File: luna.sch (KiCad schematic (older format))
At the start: 21 parts

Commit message: Almost finished.
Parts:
- C1, C2: renamed from C?; footprint (none) -> Capacitor_SMD:C_1206_3216Metric_Pad1.42x1.75mm_HandSolder
- J1: renamed from J?; footprint (none) -> Connector_PinHeader_2.54mm:PinHeader_1x06_P2.54mm_Horizontal
- J2: renamed from J?; footprint (none) -> Connector_Molex:Molex_Mini-Fit_Jr_5569-20A2_2x10_P4.20mm_Horizontal
- J3: renamed from J?; footprint (none) -> Connector_PinHeader_2.54mm:PinHeader_1x02_P2.54mm_Horizontal
- J4, J5, J6: renamed from Q?; footprint (none) -> Connector_PinHeader_2.54mm:PinHeader_1x02_P2.54mm_Horizontal
- R1, R2, R3, R4, R5, R6: renamed from R?; footprint (none) -> Resistor_SMD:R_0805_2012Metric_Pad1.15x1.40mm_HandSolder
- U1: renamed from U?; footprint (none) -> Package_TO_SOT_SMD:SOT-223-3_TabPin2
- gave numbers to parts that had none: 6
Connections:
- wire segments 79 -> 80
- no-connect marks 25 -> 40

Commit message: Second revision with on-board led swithes and dummy load output.
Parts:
- removed J2: Conn_02x10_Top_Bottom, Connector_Molex:Molex_Mini-Fit_Jr_5569-20A2_2x10_P4.20mm_Horizontal, symbol Connector_Generic:Conn_02x10_Top_Bottom
- removed J3, J4: Conn_01x02_Male, Connector_PinHeader_2.54mm:PinHeader_1x02_P2.54mm_Horizontal, symbol Connector:Conn_01x02_Male
- removed Q2, Q3: 2N7002, Package_TO_SOT_SMD:SOT-23, symbol Transistor_FET:2N7002
- removed R1: 10k, Resistor_SMD:R_0805_2012Metric_Pad1.15x1.40mm_HandSolder, symbol Device:R
- removed R3, R4: 1k, Resistor_SMD:R_0805_2012Metric_Pad1.15x1.40mm_HandSolder, symbol Device:R
- added C1, C4, C5, C6: 10u, Capacitor_SMD:C_1206_3216Metric_Pad1.42x1.75mm_HandSolder, symbol Device:C
- added D1, D2, D3: D_Schottky, Diode_SMD:D_SOD-323_HandSoldering, symbol Device:D_Schottky
- added J2: Conn_02x12_Top_Bottom, Connector_Molex:Molex_Mini-Fit_Jr_5569-24A2_2x12_P4.20mm_Horizontal, symbol Connector_Generic:Conn_02x12_Top_Bottom
- added J5: Screw_Terminal_01x06, TerminalBlock_RND:TerminalBlock_RND_205-00291_1x06_P5.08mm_Horizontal, symbol Connector:Screw_Terminal_01x06
- added Q4, Q5, Q6: DMN3404L, Package_TO_SOT_SMD:SOT-23, symbol Transistor_FET:DMN3404L
- added R10, R2, R8, R9: 10k, Resistor_SMD:R_0805_2012Metric_Pad1.15x1.40mm_HandSolder, symbol Device:R
- added R5, R6, R7: 100, Resistor_SMD:R_0805_2012Metric_Pad1.15x1.40mm_HandSolder, symbol Device:R
- R1: renamed from R5; value 10k -> 1k
- R3: renamed from R6; value 10k -> 1k
- renumbered C1 to C2, C2 to C3, J5 to J3, J6 to J4, Q4 to Q1, Q1 to Q2, Q5 to Q3, R2 to R4
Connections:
- net labels added: DUMMY_LOAD, DUMMY_LOAD_OUT, GNDPWR, LED_W1_OUT, LED_W2_OUT
- wire segments 80 -> 135
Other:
- moved on the sheet: J3, J4, Q1, Q2, Q3, R1, R3

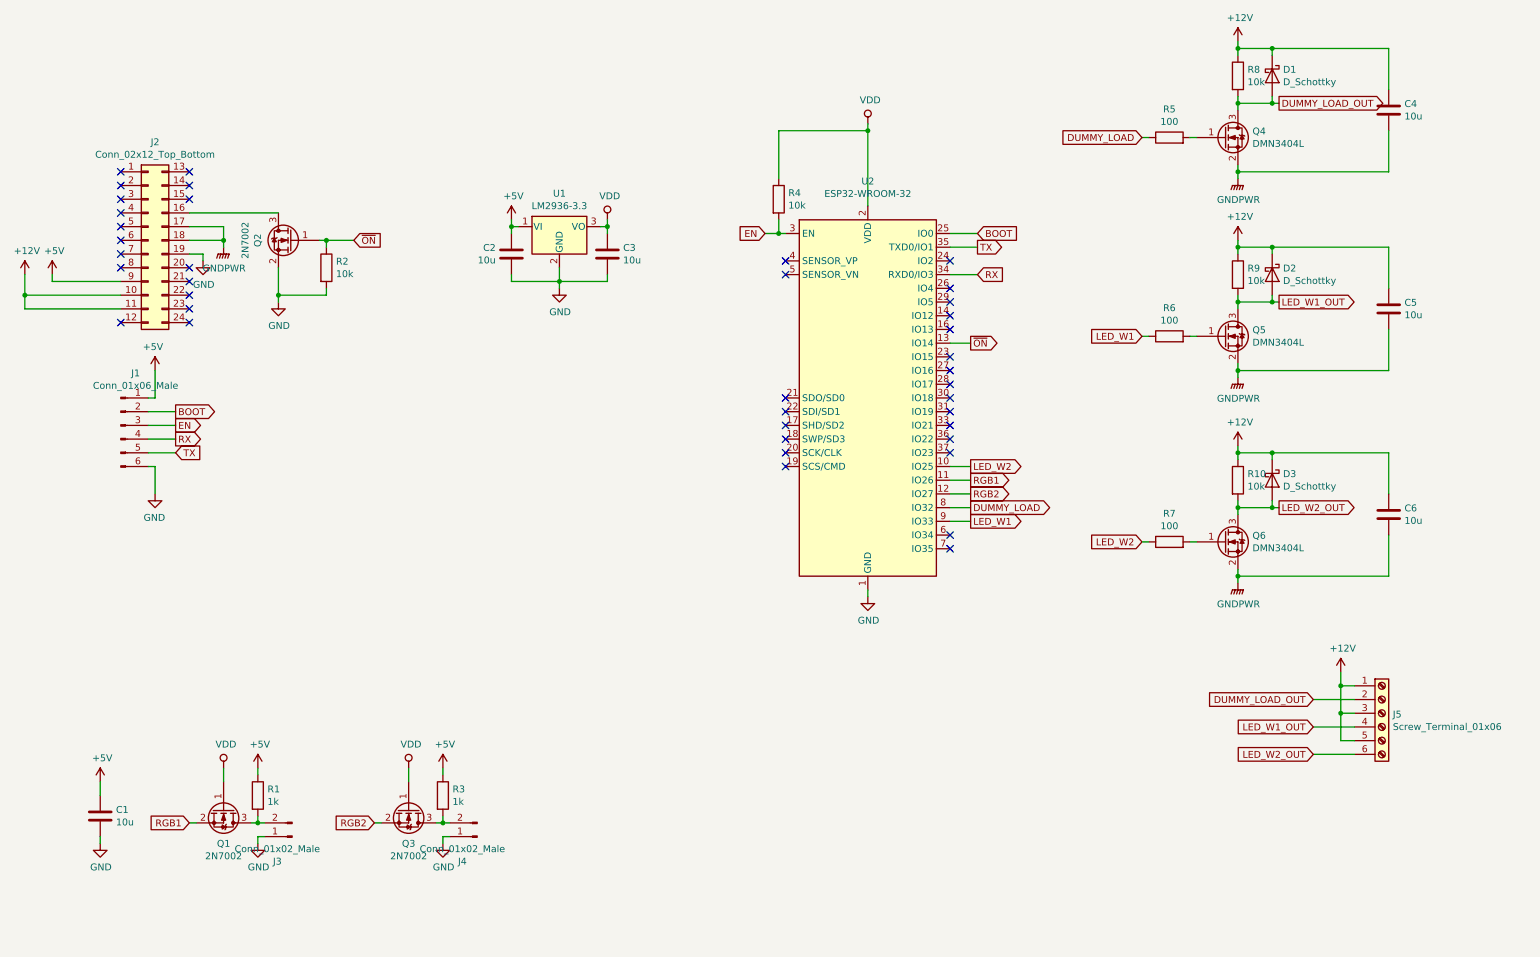
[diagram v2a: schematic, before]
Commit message: Changed voltage regulator to LD1117. Added mounting holes to schematic. Removed flyback diode and resistor from dummy driver. Removed gate resistors.
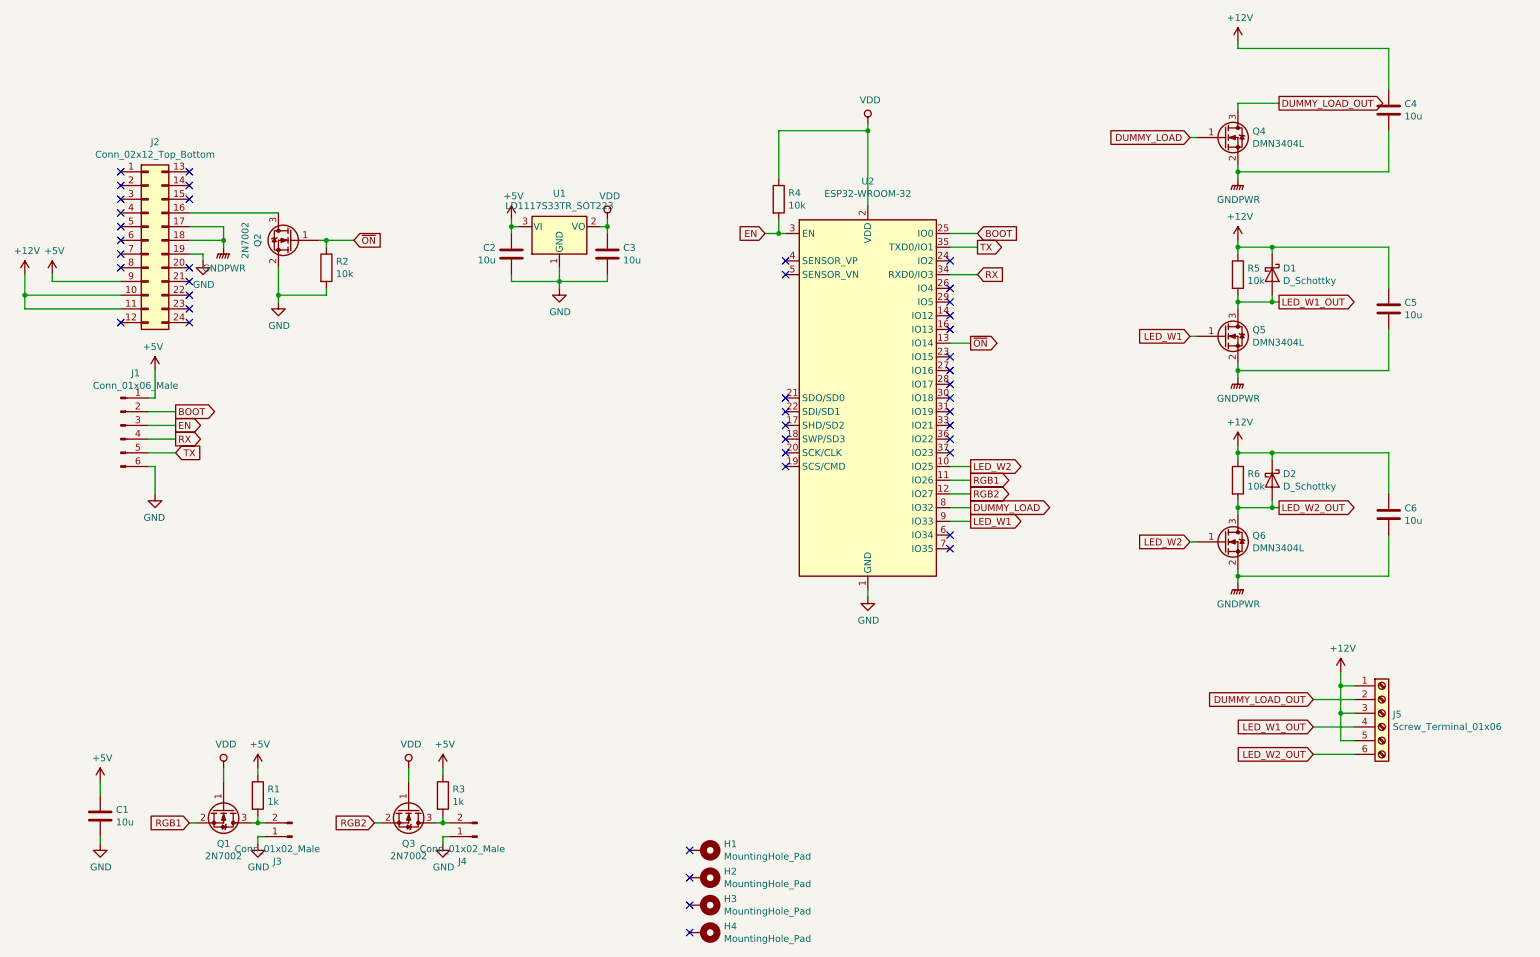
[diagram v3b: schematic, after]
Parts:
- removed D1: D_Schottky, Diode_SMD:D_SOD-323_HandSoldering, symbol Device:D_Schottky
- removed R5, R6, R7: 100, Resistor_SMD:R_0805_2012Metric_Pad1.15x1.40mm_HandSolder, symbol Device:R
- removed R8: 10k, Resistor_SMD:R_0805_2012Metric_Pad1.15x1.40mm_HandSolder, symbol Device:R
- removed U1: LM2936-3.3, Package_TO_SOT_SMD:SOT-223-3_TabPin2, symbol Regulator_Linear:LM2936-3.3
- added H1, H2, H3, H4: MountingHole_Pad, MountingHole:MountingHole_3.2mm_M3_Pad, symbol Mechanical:MountingHole_Pad
- added U1: LD1117S33TR_SOT223, Package_TO_SOT_SMD:SOT-223-3_TabPin2, symbol Regulator_Linear:LD1117S33TR_SOT223
- renumbered D2 to D1, D3 to D2, R9 to R5, R10 to R6
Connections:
- net +5V: now also U1.3 (VI)
- net DUMMY_LOAD: now also Q4.1 (G)
- net GND: now also U1.1 (GND)
- net LED_W1: now also Q5.1 (G)
- net LED_W2: now also Q6.1 (G)
- net VDD: now also U1.2 (VO)
- no-connect marks 40 -> 44
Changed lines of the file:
@@
 $EndComp
 $Comp
-L power:GND #PWR03
+L power:GND #PWR07
 U 1 1 5CCE69CC
 P 2200 2500
-F 0 "#PWR03" H 2200 2250 50  0001 C CNN
+F 0 "#PWR07" H 2200 2250 50  0001 C CNN
 F 1 "GND" H 2205 2327 50  0000 C CNN
 F 2 "" H 2200 2500 50  0001 C CNN
@@
 	2350 6200 2350 6300
 $Comp
-L power:+5V #PWR011
+L power:+5V #PWR010
 U 1 1 5CD3E2A9
 P 2600 6200
-F 0 "#PWR011" H 2600 6050 50  0001 C CNN
+F 0 "#PWR010" H 2600 6050 50  0001 C CNN
 F 1 "+5V" H 2615 6373 50  0000 C CNN
 F 2 "" H 2600 6200 50  0001 C CNN
@@
 $EndComp
 $Comp
-L power:GND #PWR012
+L power:GND #PWR011
 U 1 1 5CD3257C
 P 2600 6750
-F 0 "#PWR012" H 2600 6500 50  0001 C CNN
+F 0 "#PWR011" H 2600 6500 50  0001 C CNN
 F 1 "GND" H 2605 6577 50  0000 C CNN
 F 2 "" H 2600 6750 50  0001 C CNN
@@
 	900  2750 900  2600
 $Comp
-L Regulator_Linear:LM2936-3.3 U1
-U 1 1 5CD6EF90
-P 4800 2250
-F 0 "U1" H 4800 2492 50  0000 C CNN
-F 1 "LM2936-3.3" H 4800 2401 50  0000 C CNN
-F 2 "Package_TO_SOT_SMD:SOT-223-3_TabPin2" H 4800 2475 50  0001 C CIN
-F 3 "http://www.ti.com/lit/ds/symlink/lm2936.pdf" H 4800 2200 50  0001 C CNN
-	1    4800 2250
-	1    0    0    -1
-$EndComp
-$Comp
 L power:+5V #PWR016
 U 1 1 5CD71403
@@
 	7050 4950 7050 4900
 $Comp
-L power:GND #PWR07
+L power:GND #PWR06
 U 1 1 5CD8AC3D
 P 1850 4200
-F 0 "#PWR07" H 1850 3950 50  0001 C CNN
+F 0 "#PWR06" H 1850 3950 50  0001 C CNN
 F 1 "GND" H 1855 4027 50  0000 C CNN
 F 2 "" H 1850 4200 50  0001 C CNN
@@
 $EndComp
 $Comp
-L power:+5V #PWR06
+L power:+5V #PWR05
 U 1 1 5CD8B65E
 P 1850 3300
-F 0 "#PWR06" H 1850 3150 50  0001 C CNN
+F 0 "#PWR05" H 1850 3150 50  0001 C CNN
 F 1 "+5V" H 1865 3473 50  0000 C CNN
 F 2 "" H 1850 3300 50  0001 C CNN
@@
 Connection ~ 900  2750
 $Comp
-L power:GND #PWR010
+L power:GND #PWR012
 U 1 1 5CD6CE4D
 P 2750 2800
-F 0 "#PWR010" H 2750 2550 50  0001 C CNN
+F 0 "#PWR012" H 2750 2550 50  0001 C CNN
 F 1 "GND" H 2755 2627 50  0000 C CNN
 F 2 "" H 2750 2800 50  0001 C CNN
@@
 $EndComp
 $Comp
-L Device:R R8
-U 1 1 5CDAAC80
-P 9750 1150
-F 0 "R8" H 9820 1196 50  0000 L CNN
-F 1 "10k" H 9820 1105 50  0000 L CNN
-F 2 "Resistor_SMD:R_0805_2012Metric_Pad1.15x1.40mm_HandSolder" V 9680 1150 50  0001 C CNN
-F 3 "~" H 9750 1150 50  0001 C CNN
-	1    9750 1150
-	1    0    0    -1
-$EndComp
-$Comp
 L Connector:Screw_Terminal_01x06 J5
 U 1 1 5CDABD47
@@
 	1    0    0    -1
 $EndComp
-Text GLabel 9050 1600 0    50   Input ~ 0
+Text GLabel 9400 1600 0    50   Input ~ 0
 DUMMY_LOAD
 $Comp
@@
 $EndComp
 $Comp
-L Device:D_Schottky D1
-U 1 1 5CDB4E44
-P 10000 1150
-F 0 "D1" V 9954 1229 50  0000 L CNN
-F 1 "D_Schottky" V 10045 1229 50  0000 L CNN
-F 2 "Diode_SMD:D_SOD-323_HandSoldering" H 10000 1150 50  0001 C CNN
-F 3 "~" H 10000 1150 50  0001 C CNN
-	1    10000 1150
-	0    1    1    0
-$EndComp
-$Comp
 L power:+12V #PWR027
 U 1 1 5CDB7B0C
@@
 	9750 900  9750 950
 Wire Wire Line
-	9750 950  10000 950
-Wire Wire Line
-	10000 950  10000 1000
-Wire Wire Line
-	9750 950  9750 1000
-Connection ~ 9750 950
-Wire Wire Line
 	9750 1400 9750 1350
-Wire Wire Line
-	9750 1350 10000 1350
-Wire Wire Line
-	10000 1350 10000 1300
-Connection ~ 9750 1350
-Wire Wire Line
-	9750 1350 9750 1300
 Wire Wire Line
 	9450 1600 9400 1600
@@
 	1    0    0    -1
 $EndComp
-$Comp
-L Device:R R5
-U 1 1 5CDFD193
-P 9250 1600
-F 0 "R5" V 9457 1600 50  0000 C CNN
-F 1 "100" V 9366 1600 50  0000 C CNN
-F 2 "Resistor_SMD:R_0805_2012Metric_Pad1.15x1.40mm_HandSolder" V 9180 1600 50  0001 C CNN
-F 3 "~" H 9250 1600 50  0001 C CNN
-	1    9250 1600
-	0    -1   -1   0
-$EndComp
-Wire Wire Line
-	9100 1600 9050 1600
 Wire Wire Line
 	10850 1850 10850 1550
 Wire Wire Line
 	10850 1250 10850 950
-Wire Wire Line
-	10000 1350 10050 1350
-Connection ~ 10000 1350
 Wire Wire Line
 	9750 1800 9750 1850
@@
 Wire Wire Line
 	9750 1850 9750 1900
-Wire Wire Line
-	10000 950  10850 950
-Connection ~ 10000 950
 $Comp
 L Transistor_FET:DMN3404L Q5
@@
 $EndComp
 $Comp
-L Device:R R9
+L Device:R R5
 U 1 1 5CE2A6D1
 P 9750 2600
-F 0 "R9" H 9820 2646 50  0000 L CNN
+F 0 "R5" H 9820 2646 50  0000 L CNN
 F 1 "10k" H 9820 2555 50  0000 L CNN
 F 2 "Resistor_SMD:R_0805_2012Metric_Pad1.15x1.40mm_HandSolder" V 9680 2600 50  0001 C CNN
@@
 	1    0    0    -1
 $EndComp
-Text GLabel 9050 3050 0    50   Input ~ 0
+Text GLabel 9400 3050 0    50   Input ~ 0
 LED_W1
 $Comp
@@
 $EndComp
 $Comp
-L Device:D_Schottky D2
+L Device:D_Schottky D1
 U 1 1 5CE2A6E4
 P 10000 2600
-F 0 "D2" V 9954 2679 50  0000 L CNN
+F 0 "D1" V 9954 2679 50  0000 L CNN
 F 1 "D_Schottky" V 10045 2679 50  0000 L CNN
 F 2 "Diode_SMD:D_SOD-323_HandSoldering" H 10000 2600 50  0001 C CNN
@@
 	1    0    0    -1
 $EndComp
-$Comp
-L Device:R R6
-U 1 1 5CE2A6FB
-P 9250 3050
-F 0 "R6" V 9457 3050 50  0000 C CNN
-F 1 "100" V 9366 3050 50  0000 C CNN
-F 2 "Resistor_SMD:R_0805_2012Metric_Pad1.15x1.40mm_HandSolder" V 9180 3050 50  0001 C CNN
-F 3 "~" H 9250 3050 50  0001 C CNN
-	1    9250 3050
-	0    -1   -1   0
-$EndComp
-Wire Wire Line
-	9100 3050 9050 3050
 Wire Wire Line
 	10850 3300 10850 3000
@@
 $EndComp
 $Comp
-L Device:R R10
+L Device:R R6
 U 1 1 5CE36942
 P 9750 4100
-F 0 "R10" H 9820 4146 50  0000 L CNN
+F 0 "R6" H 9820 4146 50  0000 L CNN
 F 1 "10k" H 9820 4055 50  0000 L CNN
 F 2 "Resistor_SMD:R_0805_2012Metric_Pad1.15x1.40mm_HandSolder" V 9680 4100 50  0001 C CNN
@@
 $EndComp
 $Comp
-L Device:D_Schottky D3
+L Device:D_Schottky D2
 U 1 1 5CE36955
 P 10000 4100
-F 0 "D3" V 9954 4179 50  0000 L CNN
+F 0 "D2" V 9954 4179 50  0000 L CNN
 F 1 "D_Schottky" V 10045 4179 50  0000 L CNN
 F 2 "Diode_SMD:D_SOD-323_HandSoldering" H 10000 4100 50  0001 C CNN
@@
 	1    0    0    -1
 $EndComp
-$Comp
-L Device:R R7
-U 1 1 5CE3696C
-P 9250 4550
-F 0 "R7" V 9457 4550 50  0000 C CNN
-F 1 "100" V 9366 4550 50  0000 C CNN
-F 2 "Resistor_SMD:R_0805_2012Metric_Pad1.15x1.40mm_HandSolder" V 9180 4550 50  0001 C CNN
-F 3 "~" H 9250 4550 50  0001 C CNN
-	1    9250 4550
-	0    -1   -1   0
-$EndComp
-Wire Wire Line
-	9100 4550 9050 4550
 Wire Wire Line
 	10850 4800 10850 4500
@@
 	10000 3900 10850 3900
 Connection ~ 10000 3900
-Text GLabel 9050 4550 0    50   Input ~ 0
+Text GLabel 9400 4550 0    50   Input ~ 0
 LED_W2
 Text GLabel 10300 5700 0    50   Input ~ 0
@@
 	1450 6300 1450 6400
 $Comp
-L power:GND #PWR05
+L power:GND #PWR04
 U 1 1 5CE6634B
 P 1450 6750
-F 0 "#PWR05" H 1450 6500 50  0001 C CNN
+F 0 "#PWR04" H 1450 6500 50  0001 C CNN
 F 1 "GND" H 1455 6577 50  0000 C CNN
 F 2 "" H 1450 6750 50  0001 C CNN
@@
 NoConn ~ 2100 2850
 $Comp
-L power:+5V #PWR0101
+L power:+5V #PWR03
 U 1 1 5CFE181B
 P 1450 6300
-F 0 "#PWR0101" H 1450 6150 50  0001 C CNN
+F 0 "#PWR03" H 1450 6150 50  0001 C CNN
 F 1 "+5V" H 1465 6473 50  0000 C CNN
 F 2 "" H 1450 6300 50  0001 C CNN
@@
 	2350 2250 2350 2350
 Connection ~ 2350 2350
+$Comp
+L Mechanical:MountingHole_Pad H1
+U 1 1 5CDD5A73
+P 5850 6800
+F 0 "H1" V 5804 6950 50  0000 L CNN
+F 1 "MountingHole_Pad" V 5895 6950 50  0000 L CNN
+F 2 "MountingHole:MountingHole_3.2mm_M3_Pad" H 5850 6800 50  0001 C CNN
+F 3 "~" H 5850 6800 50  0001 C CNN
+	1    5850 6800
+	0    1    1    0
+$EndComp
+$Comp
+L Mechanical:MountingHole_Pad H2
+U 1 1 5CDD8186
+P 5850 7000
+F 0 "H2" V 5804 7150 50  0000 L CNN
+F 1 "MountingHole_Pad" V 5895 7150 50  0000 L CNN
+F 2 "MountingHole:MountingHole_3.2mm_M3_Pad" H 5850 7000 50  0001 C CNN
+F 3 "~" H 5850 7000 50  0001 C CNN
+	1    5850 7000
+	0    1    1    0
+$EndComp
+$Comp
+L Mechanical:MountingHole_Pad H3
+U 1 1 5CDD83FB
+P 5850 7200
+F 0 "H3" V 5804 7350 50  0000 L CNN
+F 1 "MountingHole_Pad" V 5895 7350 50  0000 L CNN
+F 2 "MountingHole:MountingHole_3.2mm_M3_Pad" H 5850 7200 50  0001 C CNN
+F 3 "~" H 5850 7200 50  0001 C CNN
+	1    5850 7200
+	0    1    1    0
+$EndComp
+$Comp
+L Mechanical:MountingHole_Pad H4
+U 1 1 5CDD86EA
+P 5850 7400
+F 0 "H4" V 5804 7550 50  0000 L CNN
+F 1 "MountingHole_Pad" V 5895 7550 50  0000 L CNN
+F 2 "MountingHole:MountingHole_3.2mm_M3_Pad" H 5850 7400 50  0001 C CNN
+F 3 "~" H 5850 7400 50  0001 C CNN
+	1    5850 7400
+	0    1    1    0
+$EndComp
+$Comp
+L Regulator_Linear:LD1117S33TR_SOT223 U1
+U 1 1 5CDF6D57
+P 4800 2250
+F 0 "U1" H 4800 2492 50  0000 C CNN
+F 1 "LD1117S33TR_SOT223" H 4800 2401 50  0000 C CNN
+F 2 "Package_TO_SOT_SMD:SOT-223-3_TabPin2" H 4800 2450 50  0001 C CNN
+F 3 "http://www.st.com/st-web-ui/static/active/en/resource/technical/document/datasheet/CD00000544.pdf" H 4900 2000 50  0001 C CNN
+	1    4800 2250
+	1    0    0    -1
+$EndComp
+NoConn ~ 5750 6800
+NoConn ~ 5750 7000
+NoConn ~ 5750 7200
+NoConn ~ 5750 7400
+Wire Wire Line
+	9750 1350 10050 1350
+Wire Wire Line
+	9750 950  10850 950
 $EndSCHEMATC
